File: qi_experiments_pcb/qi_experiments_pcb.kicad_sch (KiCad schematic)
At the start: 70 parts, among them J1 Conn_01x03, J2 USB_C_Receptacle_USB2.0, J3 Conn_01x02, J4 Conn_01x02, Q1 2N7002, Q2 2N7002, Q3 2N7002, U2 SPX3819M5-L-3-3, U4 AP62200Z6, U5 CH340N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

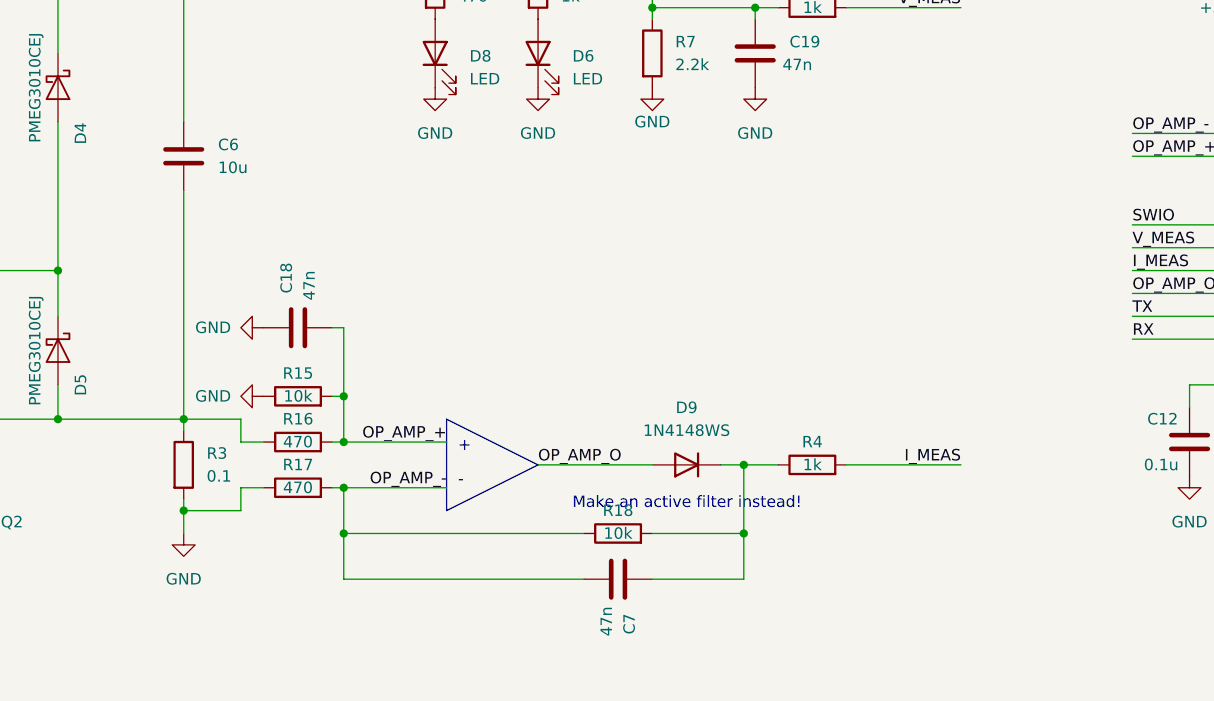
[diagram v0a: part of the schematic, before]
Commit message: curent sensing amp polarity swap
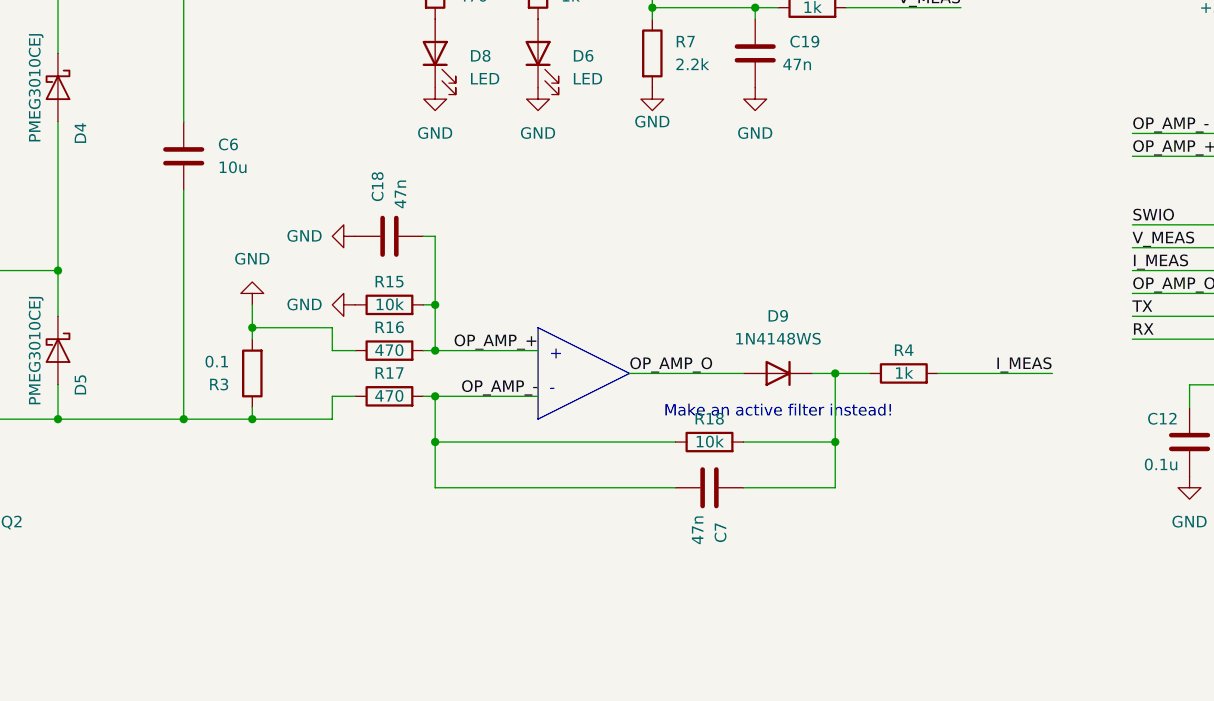
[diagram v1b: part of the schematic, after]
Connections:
- net GND: now also R16.1; no longer R17.1
- net at C6.2, D1.2 (A), D3.2 (A)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: now also R17.1; no longer R16.1
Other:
- moved on the sheet: C18, C7, D9, R15, R16, R17, R18, R3, R4
